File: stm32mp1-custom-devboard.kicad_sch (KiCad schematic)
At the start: 12 parts, among them P1 Main Power Supply, U10 APX803D-29SRG-7

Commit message: Started issues implementation
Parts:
- added D6, D7, D8: KPT-1608CGCK, Diodes:LED_KPT-1608CGCK, symbol Diodes:KPT-1608CGCK
- added R64, R65, R66: 220R, Resistor_Smd_0603:220R_0603, symbol Resistors_Smd0603:220R
- added R67: 0R, Resistor_Smd_0603:0R_0603, symbol Resistors_Smd0603:0R
- added R68, R69: 10k, Resistor_Smd_0603:10k_0603, symbol Resistors_Smd0603:10k
- added Sw1, Sw2: 434153017835, Microswitches:434153017835, symbol Microswitches:434153017835
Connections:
- net 3V3: now also D6.1 (A), D7.1 (A), D8.1 (A), R68.1, R69.1
- net Arduino Shield Module/ATN: no longer R57.1
- net GND: now also R67.1, Sw1.2, Sw1.4, Sw2.2, Sw2.4
- net MiniPci Module/SPDT_SEL-~WDISABLE~: now also R67.2
- net RESET renamed STM32MP1 module/STM32-~RST~
- new net: D7.2 (K), R65.2
- new net: R69.2, Sw2.3
- new net: R68.2, Sw1.3
- new net: D8.2 (K), R66.2
- new net: D6.2 (K), R64.2
- new net STM32MP1 module/I2C6-SDA: Sw2.1
- new net STM32MP1 module/PC7-GPIO: R64.1
- new net STM32MP1 module/PD14-GPIO: R66.1
- new net STM32MP1 module/PE14-GPIO: R57.1
- new net STM32MP1 module/PE3-GPIO: R65.1
- no-connect marks 6 -> 0
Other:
- sheet MiniPci Module ports: added none; removed I2C-SCL, I2C-SDA, NETLIGHT, PCM_IN, PCM_OUT, PCM_SYNC, PWRKEY, TRX_SWITCH-PCM_CLK, UART_CTS, UART_DCD, UART_DTR, UART_RI, UART_RTS, UART_RX, UART_TX
- sheet STM32MP1 module ports: added PD14-GPIO, PE0-GPIO, PE1-GPIO, PG7-GPIO; removed UART8-CTS, UART8-RTS, UART8-RXD, UART8-TXD

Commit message: Tracking finished
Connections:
- net STM32MP1 module/I2C6-SCL: now also Sw1.1
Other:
- sheet MiniPci Module ports: added none; removed USB-D_M, USB-D_P
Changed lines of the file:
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@@
   (junction (at 109.22 43.18) (diameter 1.016) (color 0 0 0 0))
   (junction (at 172.72 76.2) (diameter 1.016) (color 0 0 0 0))
-  (junction (at 261.62 153.67) (diameter 1.016) (color 0 0 0 0))
-  (junction (at 264.16 151.13) (diameter 1.016) (color 0 0 0 0))
   (wire (pts (xy 78.74 67.31) (xy 78.74 66.04))
     (stroke (width 0) (type solid) (color 0 0 0 0))
@@
     (stroke (width 0) (type solid) (color 0 0 0 0))
   )
-  (wire (pts (xy 238.76 151.13) (xy 264.16 151.13))
+  (wire (pts (xy 238.76 151.13) (xy 270.51 151.13))
+    (stroke (width 0) (type solid) (color 0 0 0 0))
+  )
+  (wire (pts (xy 238.76 153.67) (xy 270.51 153.67))
     (stroke (width 0) (type solid) (color 0 0 0 0))
   )
@@
     (stroke (width 0) (type solid) (color 0 0 0 0))
   )
-  (wire (pts (xy 261.62 153.67) (xy 238.76 153.67))
-    (stroke (width 0) (type solid) (color 0 0 0 0))
-  )
-  (wire (pts (xy 261.62 153.67) (xy 261.62 167.64))
-    (stroke (width 0) (type solid) (color 0 0 0 0))
-  )
-  (wire (pts (xy 261.62 167.64) (xy 270.51 167.64))
-    (stroke (width 0) (type solid) (color 0 0 0 0))
-  )
-  (wire (pts (xy 264.16 151.13) (xy 270.51 151.13))
-    (stroke (width 0) (type solid) (color 0 0 0 0))
-  )
-  (wire (pts (xy 264.16 165.1) (xy 264.16 151.13))
-    (stroke (width 0) (type solid) (color 0 0 0 0))
-  )
   (wire (pts (xy 264.16 217.17) (xy 265.43 217.17))
     (stroke (width 0) (type solid) (color 0 0 0 0))
@@
     (stroke (width 0) (type solid) (color 0 0 0 0))
   )
-  (wire (pts (xy 270.51 153.67) (xy 261.62 153.67))
-    (stroke (width 0) (type solid) (color 0 0 0 0))
-  )
-  (wire (pts (xy 270.51 165.1) (xy 264.16 165.1))
-    (stroke (width 0) (type solid) (color 0 0 0 0))
-  )
   (wire (pts (xy 270.51 171.45) (xy 238.76 171.45))
     (stroke (width 0) (type solid) (color 0 0 0 0))
@@
     (stroke (width 0) (type solid) (color 0 0 0 0))
   )
+  (wire (pts (xy 302.26 207.01) (xy 349.25 207.01))
+    (stroke (width 0) (type solid) (color 0 0 0 0))
+  )
   (wire (pts (xy 317.5 102.87) (xy 320.04 102.87))
     (stroke (width 0) (type solid) (color 0 0 0 0))
@@
   )
   (wire (pts (xy 330.2 130.81) (xy 317.5 130.81))
-    (stroke (width 0) (type solid) (color 0 0 0 0))
-  )
-  (wire (pts (xy 347.98 207.01) (xy 302.26 207.01))
     (stroke (width 0) (type solid) (color 0 0 0 0))
   )
@@
       (effects (font (size 1.27 1.27)) (justify left))
     )
-    (pin "USB-D_M" bidirectional (at 270.51 165.1 180)
-      (effects (font (size 1.27 1.27)) (justify left))
-    )
-    (pin "USB-D_P" bidirectional (at 270.51 167.64 180)
-      (effects (font (size 1.27 1.27)) (justify left))
-    )

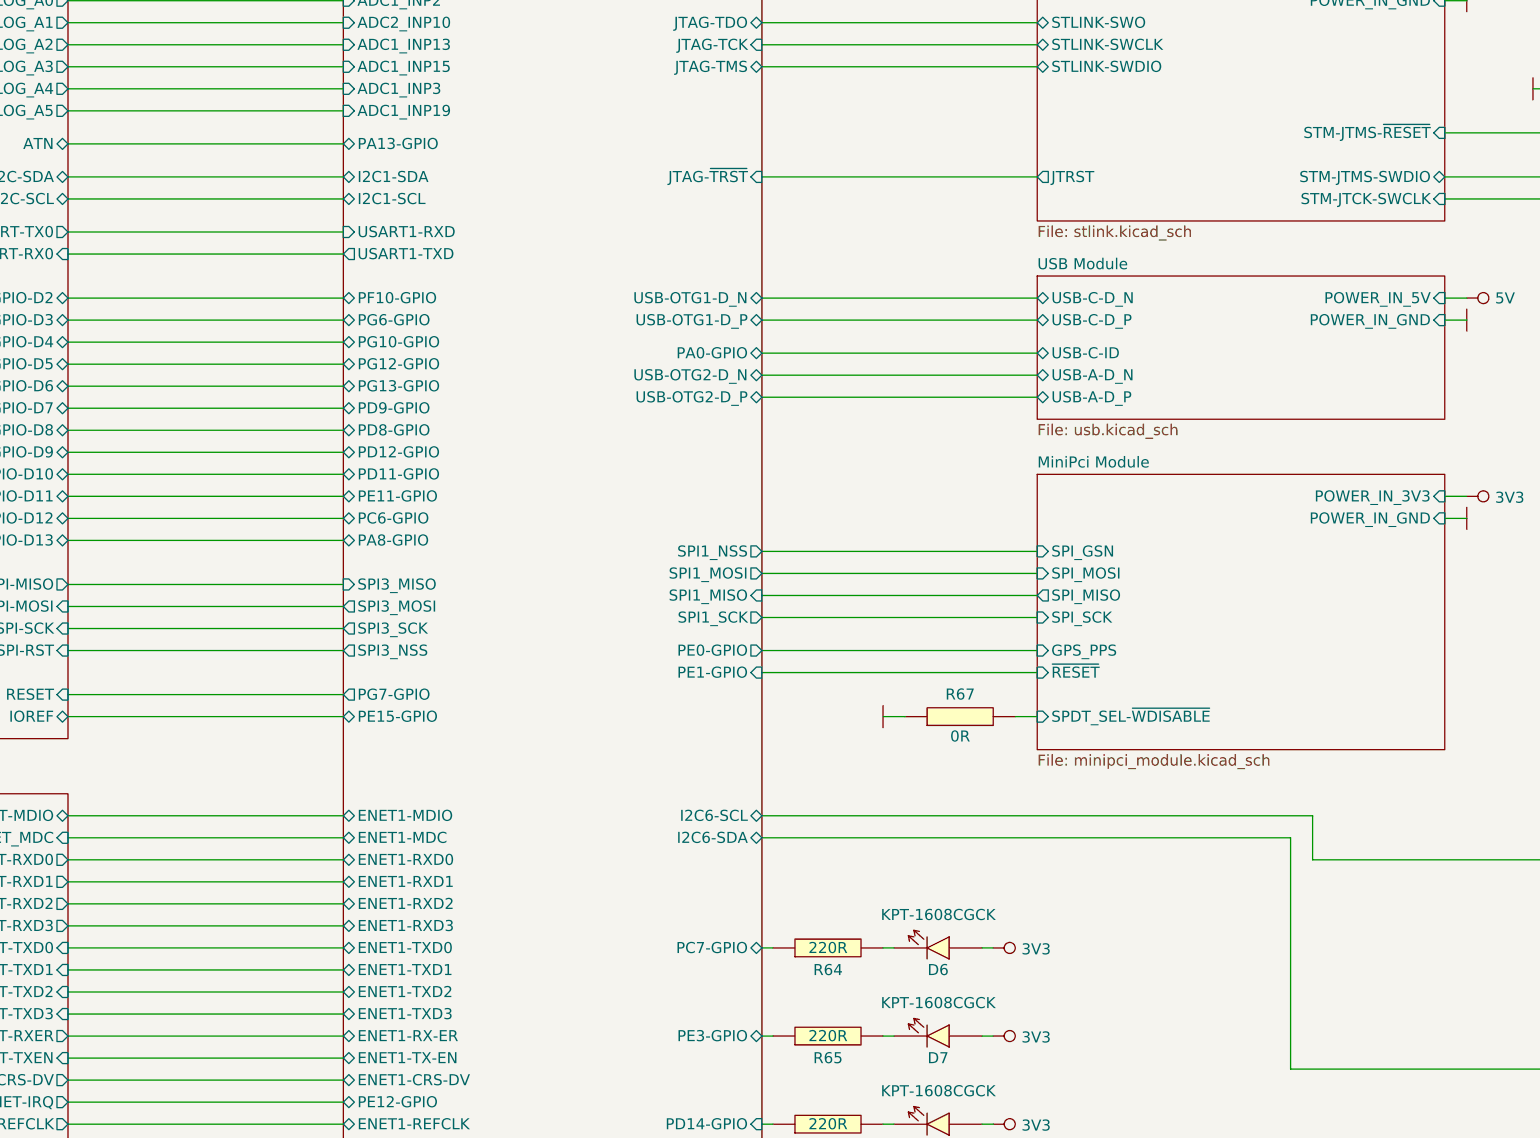
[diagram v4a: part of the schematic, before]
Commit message: Reworked schematic and applied changes on pcb related with mini pci express
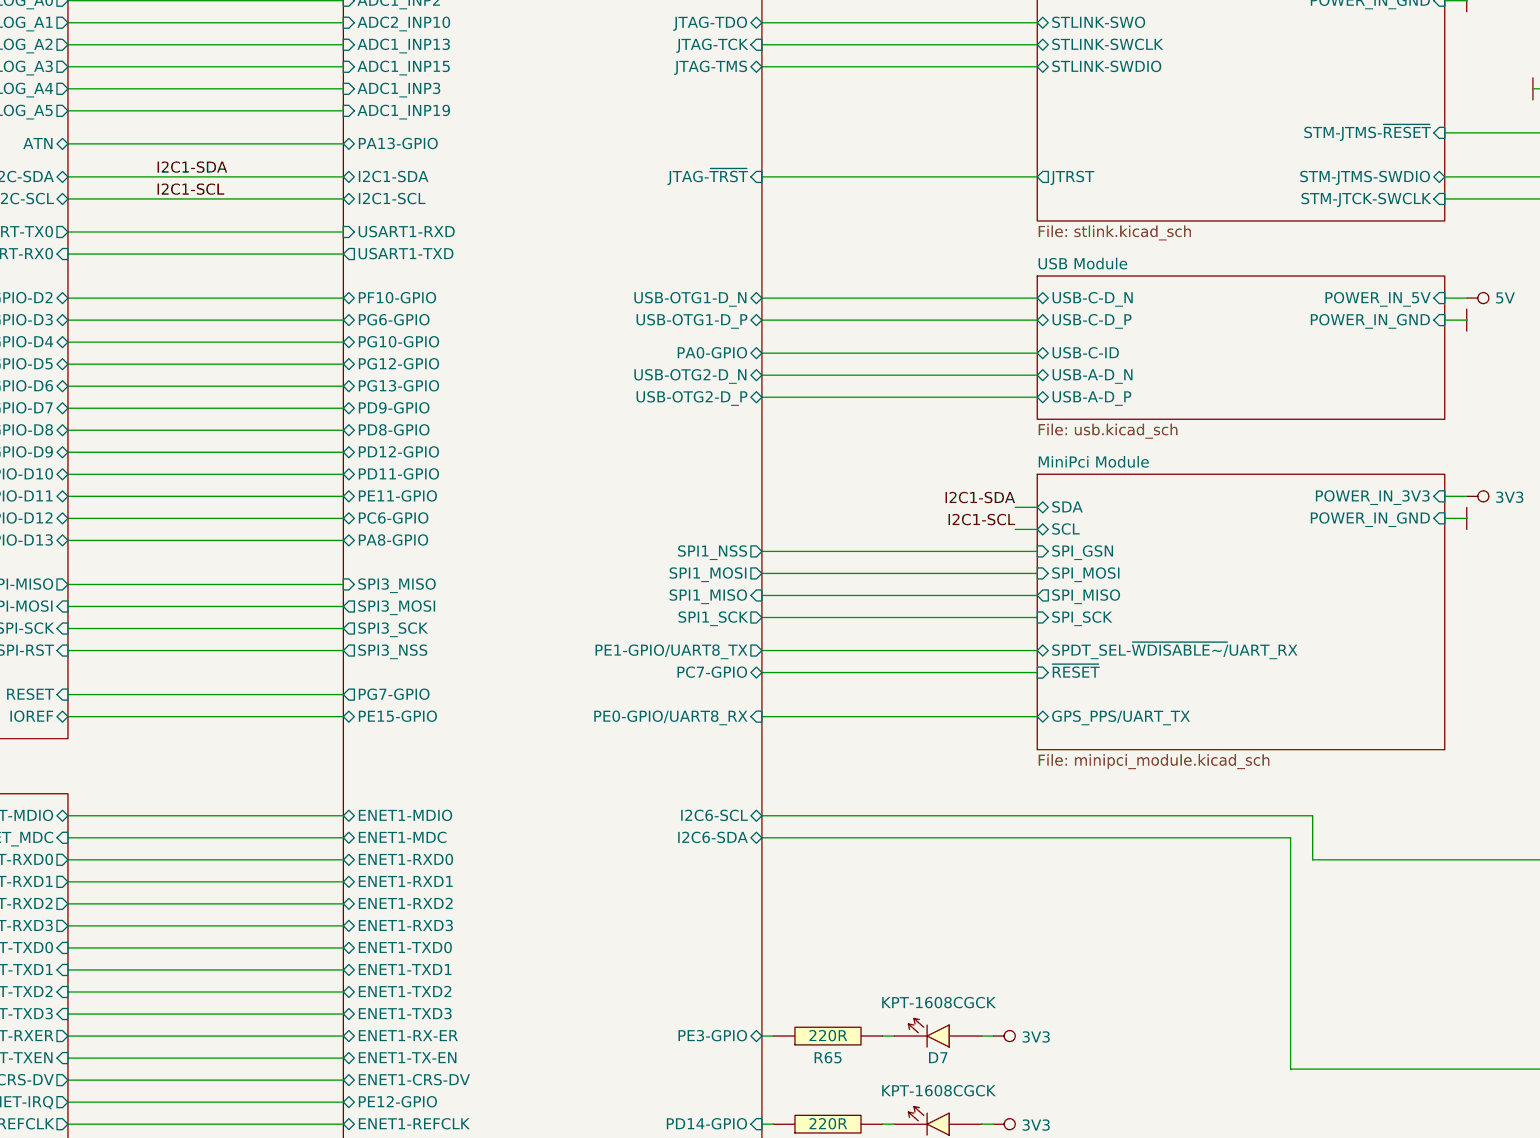
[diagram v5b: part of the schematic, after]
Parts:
- removed D6: KPT-1608CGCK, Diodes:LED_KPT-1608CGCK, symbol Diodes:KPT-1608CGCK
- removed R64: 220R, Resistor_Smd_0603:220R_0603, symbol Resistors_Smd0603:220R
- removed R67: 0R, Resistor_Smd_0603:0R_0603, symbol Resistors_Smd0603:0R
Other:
- sheet MiniPci Module ports: added GPS_PPS/UART_TX, SCL, SDA, SPDT_SEL-~WDISABLE~/UART_RX; removed GPS_PPS, SPDT_SEL-~WDISABLE~
- sheet STM32MP1 module ports: added PE0-GPIO/UART8_RX, PE1-GPIO/UART8_TX; removed PE0-GPIO, PE1-GPIO

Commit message: Updated schematic and pdf
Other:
- sheet STM32MP1 module ports: added PG14-GPIO; removed PG13-GPIO

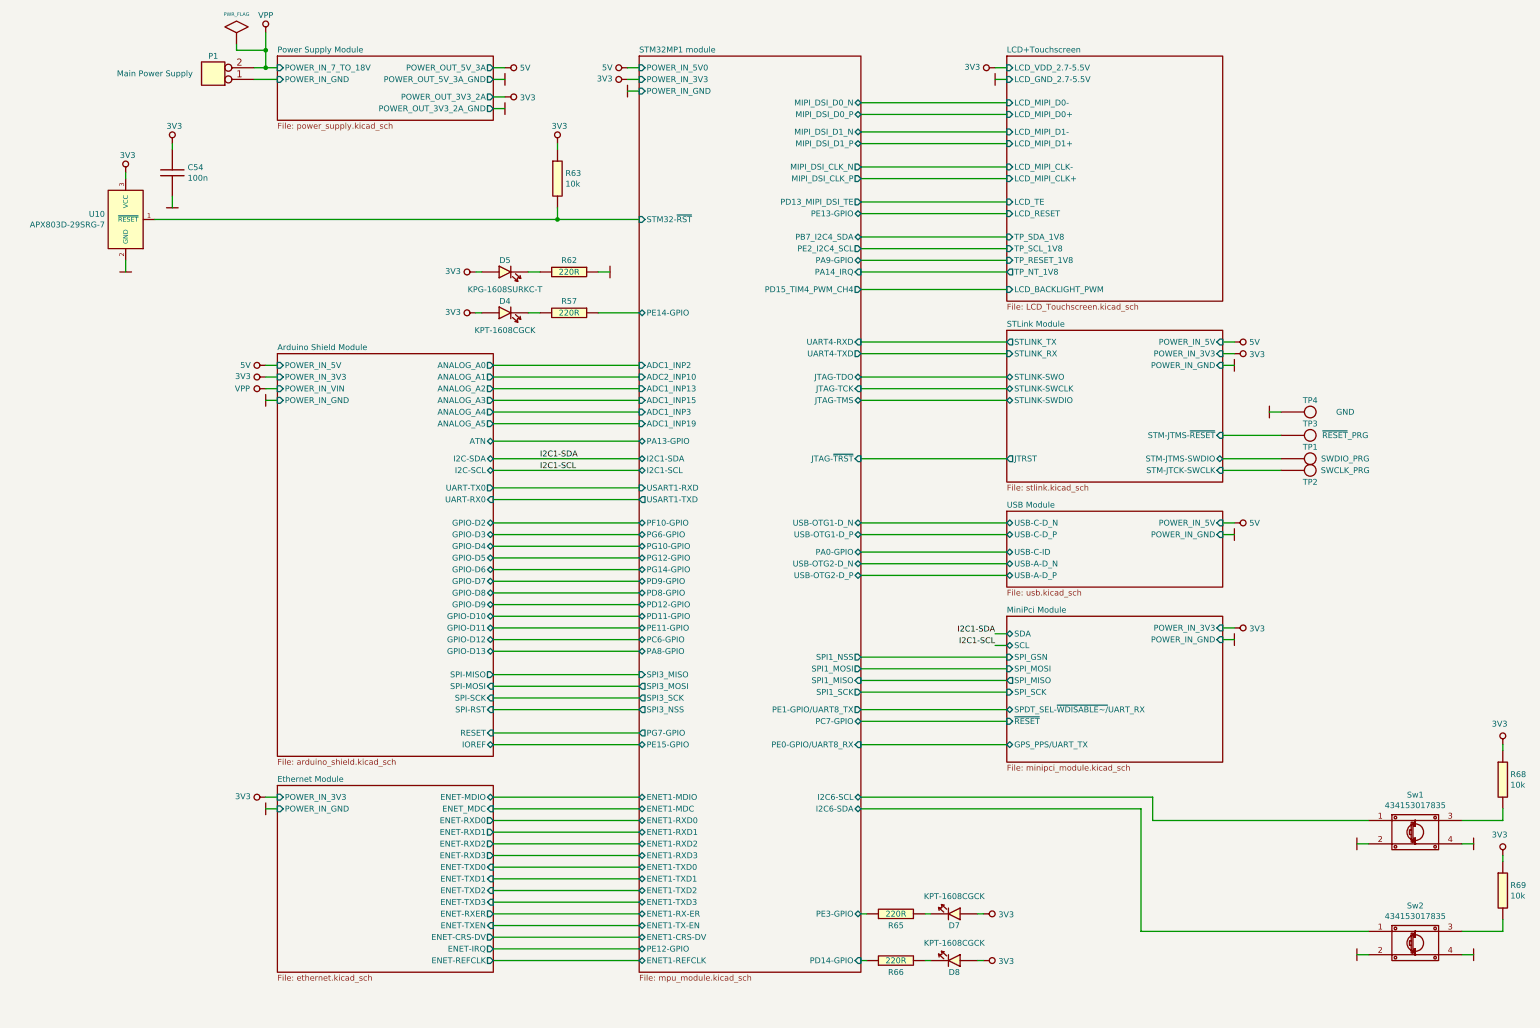
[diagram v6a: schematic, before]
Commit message: Modified ethernet
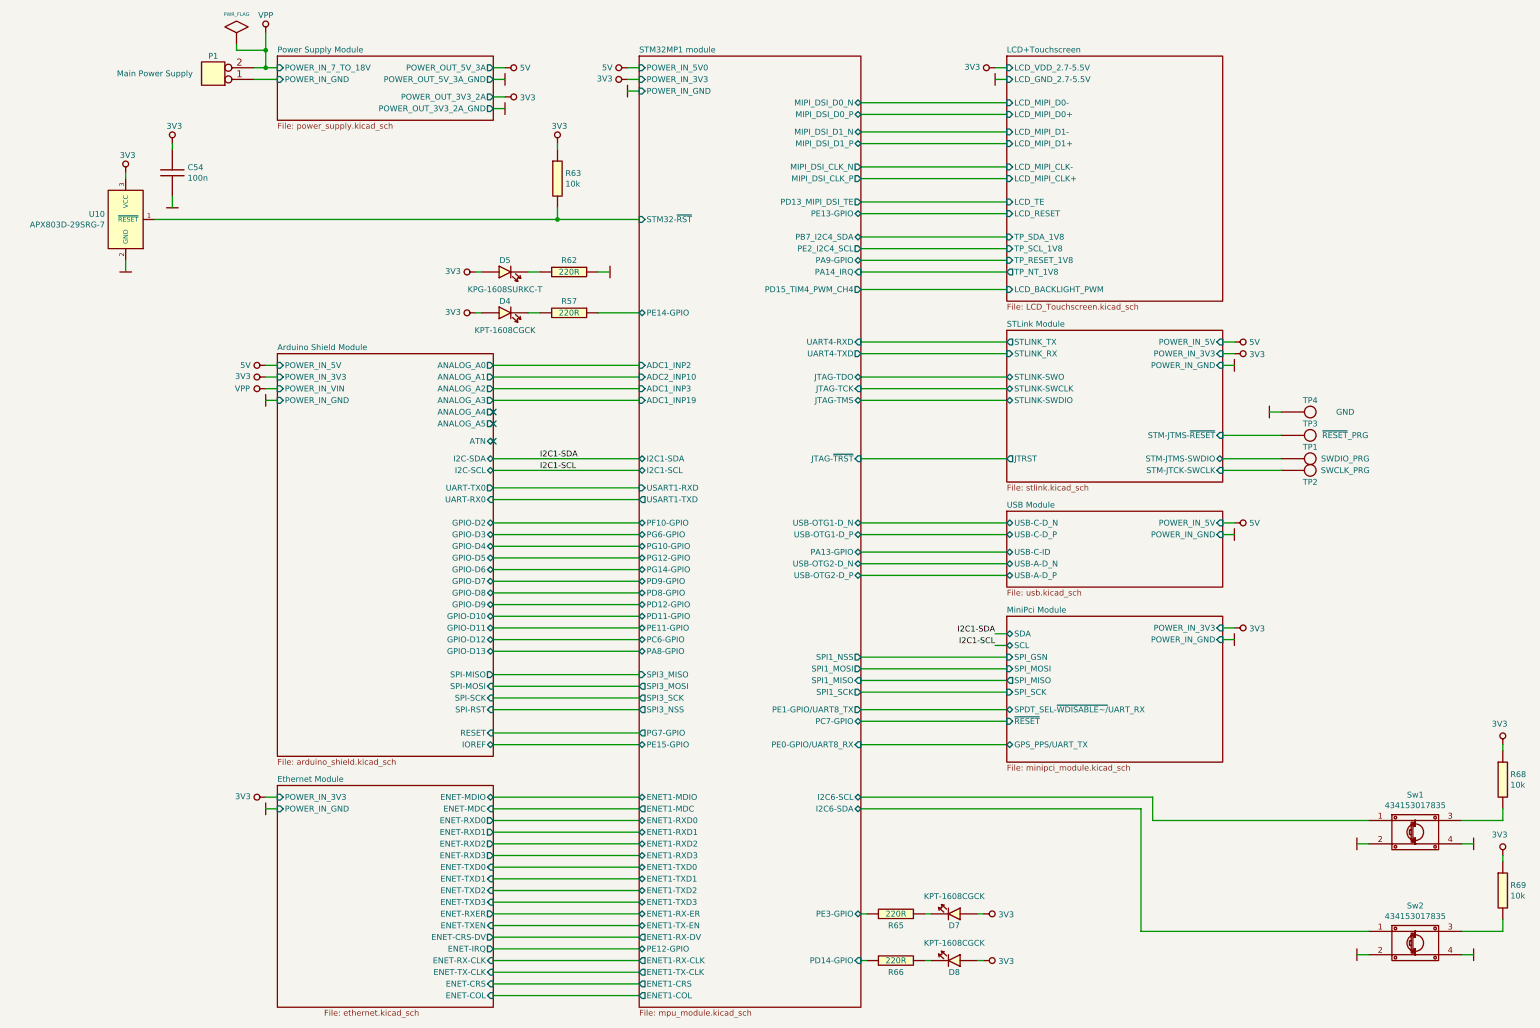
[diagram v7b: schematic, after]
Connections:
- no-connect marks 0 -> 3
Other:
- sheet Ethernet Module ports: added ENET-COL, ENET-CRS, ENET-MDC, ENET-RX-CLK, ENET-TX-CLK; removed ENET-REFCLK, ENET_MDC
- sheet STM32MP1 module ports: added ENET1-COL, ENET1-CRS, ENET1-RX-CLK, ENET1-RX-DV, ENET1-TX-CLK; removed ADC1_INP13, ADC1_INP15, ENET1-CRS-DV, ENET1-REFCLK, PA0-GPIO
